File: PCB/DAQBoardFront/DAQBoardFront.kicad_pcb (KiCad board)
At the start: 2 copper layers, 69.8 x 64.2 mm, 35 parts, among them IC2 LMR51430YDDCR, J2 53375-0410, T1 AC1210-110-C, U5 TCAN1051VDRQ1

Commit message: Nearly functional DAQ boards with buck converters and SMD CAN modules
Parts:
- D3, D4, R10, R13, R14, R7, R8, R9, U5: moved to B.Cu
- T1: value AC1210-110-C -> ~; moved to B.Cu
- moved R8 30.4 mm to (141.1, 87.8), turned to 90 degrees
- moved R10 28.3 mm to (143.8, 90.3), turned to 90 degrees
- moved R6 25.7 mm to (138.6, 99.0)
- moved D3 23.0 mm to (143.2, 84.2), turned to 90 degrees
- moved C5 21.2 mm to (141.2, 99.0)
- moved D4 20.9 mm to (145.9, 86.7), turned to 90 degrees
- moved L3 19.8 mm to (141.4, 108.8)
- moved R3 19.8 mm to (141.4, 104.6)
- moved C4 16.1 mm to (143.9, 104.6)
- moved L2 15.4 mm to (143.8, 116.0)
- moved R2 15.4 mm to (143.8, 111.8)
- moved R5 15.0 mm to (138.2, 85.6)
- moved D2 13.9 mm to (140.4, 82.0), turned to 90 degrees
- moved C3 13.8 mm to (145.9, 111.8)
- moved U5 11.5 mm to (114.2, 75.7), turned to 180 degrees
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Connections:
- J1 pad 1: /ExtraAnalog -> /FRSus
- J1 pad 2: /SteeringAngle -> /FLSus
- J1 pad 3: /FLSus -> /SteeringAngle
- J1 pad 4: /FRSus -> /ExtraAnalog
- R13 pad 1: Net-(T1-AB) -> Net-(T1-AA)
- R14 pad 2: Net-(T1-SA) -> Net-(T1-SB)
- T1 pad 1: /CAN Hi -> Net-(T1-AA)
- T1 pad 2: Net-(T1-AB) -> Net-(T1-SB)
- T1 pad 3: Net-(T1-SA) -> /CAN Lo
- T1 pad 4: /CAN Lo -> /CAN Hi
- U5 pad 6: Net-(T1-SA) -> Net-(T1-SB)
- U5 pad 7: Net-(T1-AB) -> Net-(T1-AA)
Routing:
- net /+3.3V: track 5.16 -> 81.3 mm, vias 0 -> 1
- net +5V: track 49.4 -> 79.4 mm
- net /ExtraAnalog: track 74.3 -> 53.5 mm
- net /FLSus: track 58.4 -> 40.8 mm
- net /SteeringAngle: track 63.7 -> 47.5 mm
- net /CAN Hi: track 0.00 -> 14.8 mm
- net /Brake P Input (12V): track 63.5 -> 49.4 mm
- net Net-(D3-A): track 0.00 -> 12.6 mm
- net /CAN Lo: track 0.00 -> 10.5 mm
- net Net-(D4-A): track 0.00 -> 10.5 mm
- net Net-(D2-A): track 5.85 -> 16.1 mm
- net /CANRx: track 12.4 -> 21.3 mm
- net /FLHallEffect: track 55.9 -> 48.3 mm, vias 0 -> 1
- net Net-(T1-AA): track 0.00 -> 5.45 mm
- net Net-(T1-SB): track 0.00 -> 5.45 mm
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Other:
- board size 69.8 x 64.2 mm -> 61.8 x 64.2 mm

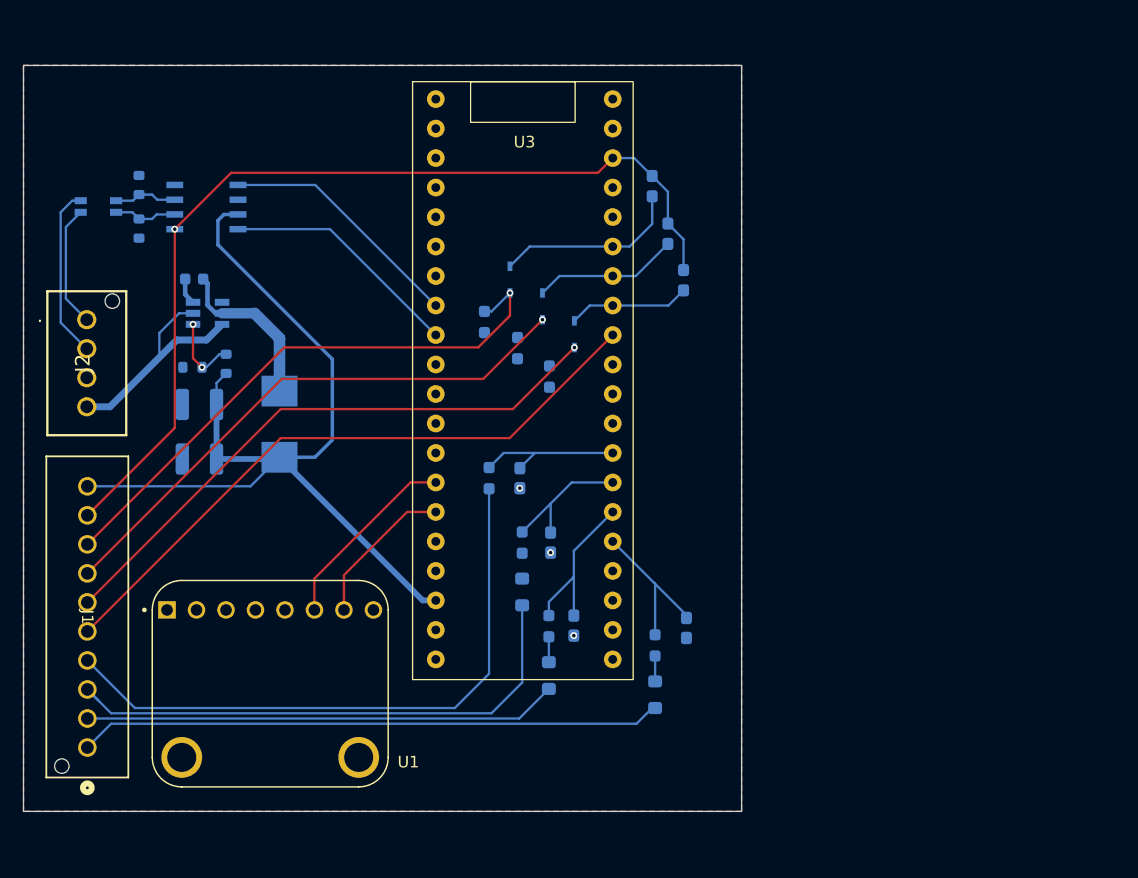
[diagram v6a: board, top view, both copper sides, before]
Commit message: Added schematic design for current sense amplifier
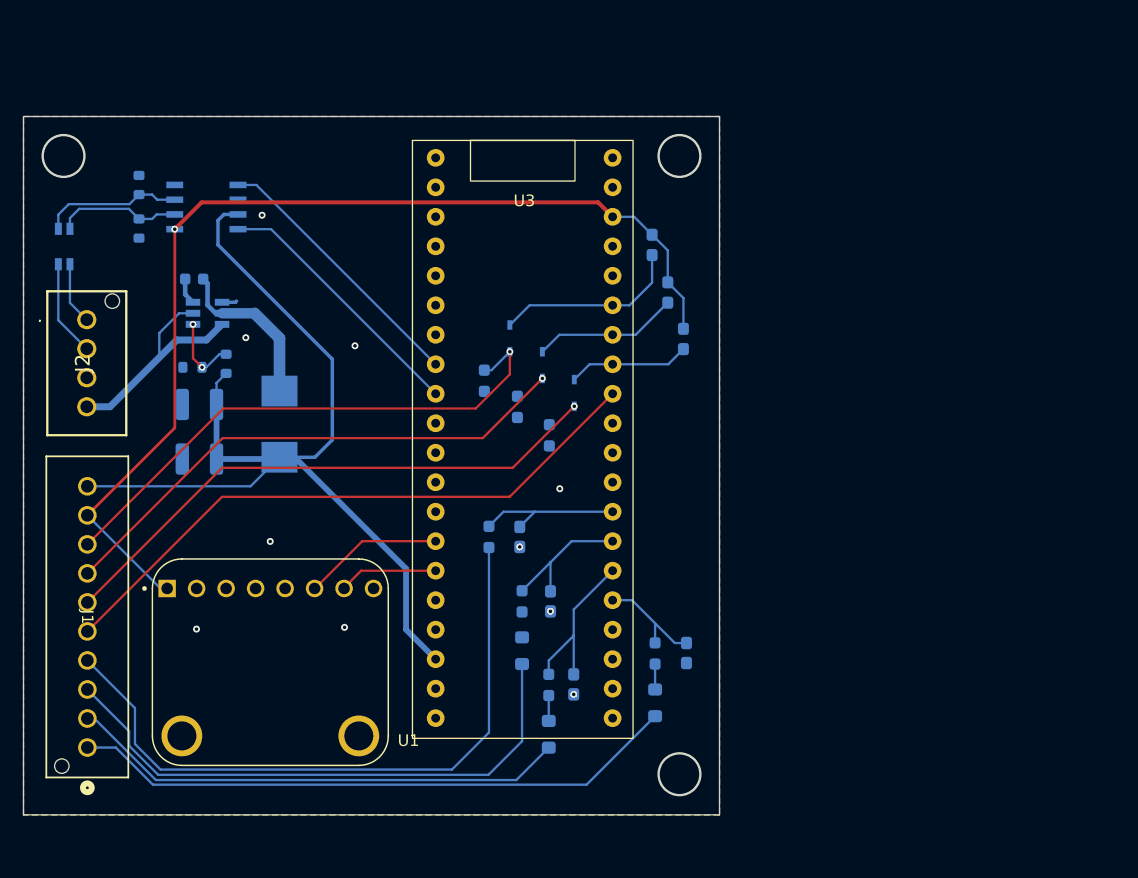
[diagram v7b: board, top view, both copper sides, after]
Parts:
- moved T1 5.53 mm to (101.5, 77.6), turned to -90 degrees
- moved C3 5.06 mm to (145.9, 116.8)
- moved C4 5.06 mm to (143.9, 109.7)
- moved C5 5.06 mm to (141.2, 104.1)
- moved D2 5.06 mm to (140.4, 87.0)
- moved D3 5.06 mm to (143.2, 89.3)
- moved L2 5.06 mm to (143.7, 121.1)
- moved L3 5.06 mm to (141.4, 113.9)
- moved R10 5.06 mm to (143.8, 95.4)
- moved R2 5.06 mm to (143.7, 116.9)
- moved R3 5.06 mm to (141.4, 109.7)
- moved R5 5.06 mm to (138.2, 90.7)
- moved R6 5.06 mm to (138.6, 104.1)
- moved R7 5.06 mm to (154.0, 83.1)
- moved R8 5.06 mm to (141.0, 92.9)
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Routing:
- net /+3.3V: track 81.3 -> 89.7 mm
- net Net-(T1-AA): track 5.45 -> 12.1 mm
- net /CAN Hi: track 14.8 -> 8.29 mm
- net Net-(T1-SB): track 5.45 -> 10.8 mm
- net +5V: track 79.4 -> 84.6 mm
- net /CAN Lo: track 10.5 -> 5.38 mm
- net /Acc SCL: track 16.6 -> 12.1 mm
- net /Acc SDA: track 13.2 -> 8.78 mm
- net /ExtraAnalog: track 53.5 -> 57.6 mm
- net Net-(U3-A0): track 13.7 -> 9.68 mm
- net /FRSus: track 50.3 -> 52.7 mm
- net /FLSus: track 40.8 -> 43.1 mm
- net /Brake P Input (12V): track 49.4 -> 47.3 mm
- net /FRHallEffect: track 51.0 -> 48.9 mm
- net /FLHallEffect: track 48.3 -> 46.1 mm
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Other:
- board size 61.8 x 64.2 mm -> 59.9 x 60.2 mm

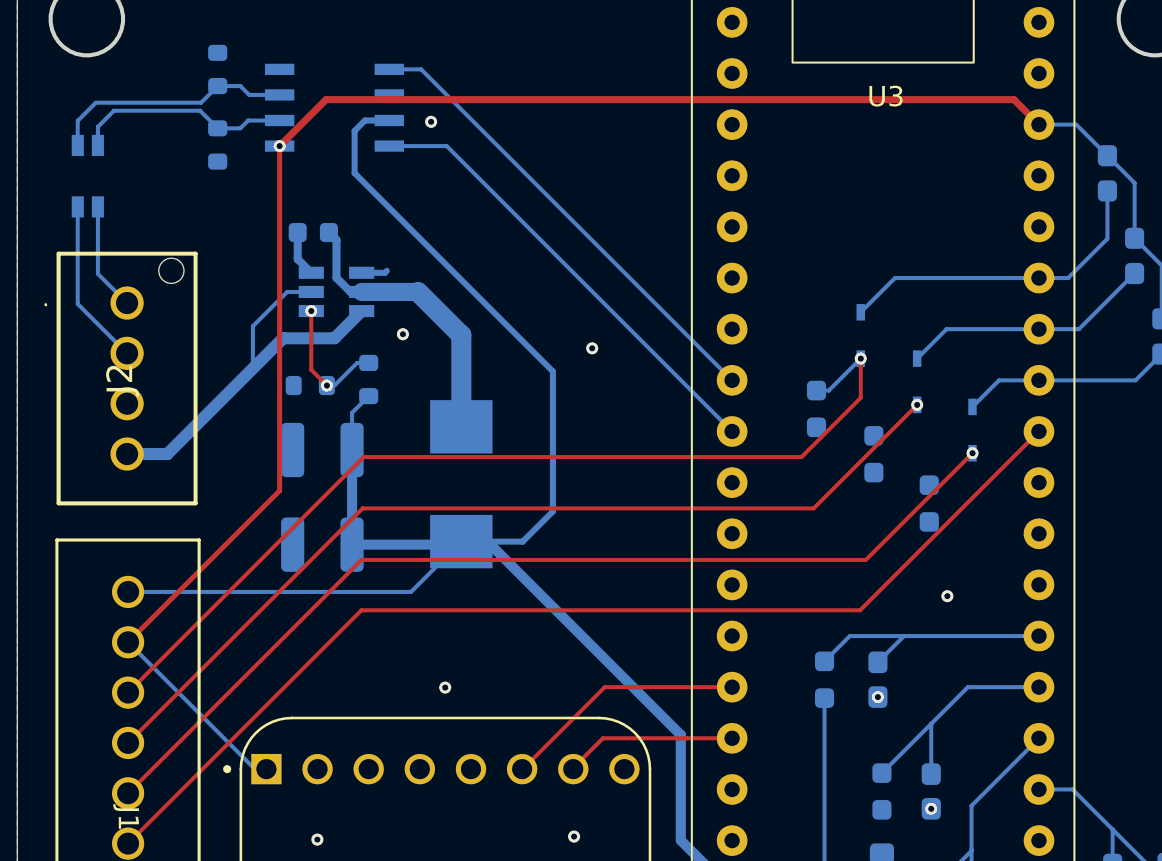
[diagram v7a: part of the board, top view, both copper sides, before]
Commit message: Completed V2.0 of DAQ board, including buck converter, input current measurement, and onboard CAN Transceiver
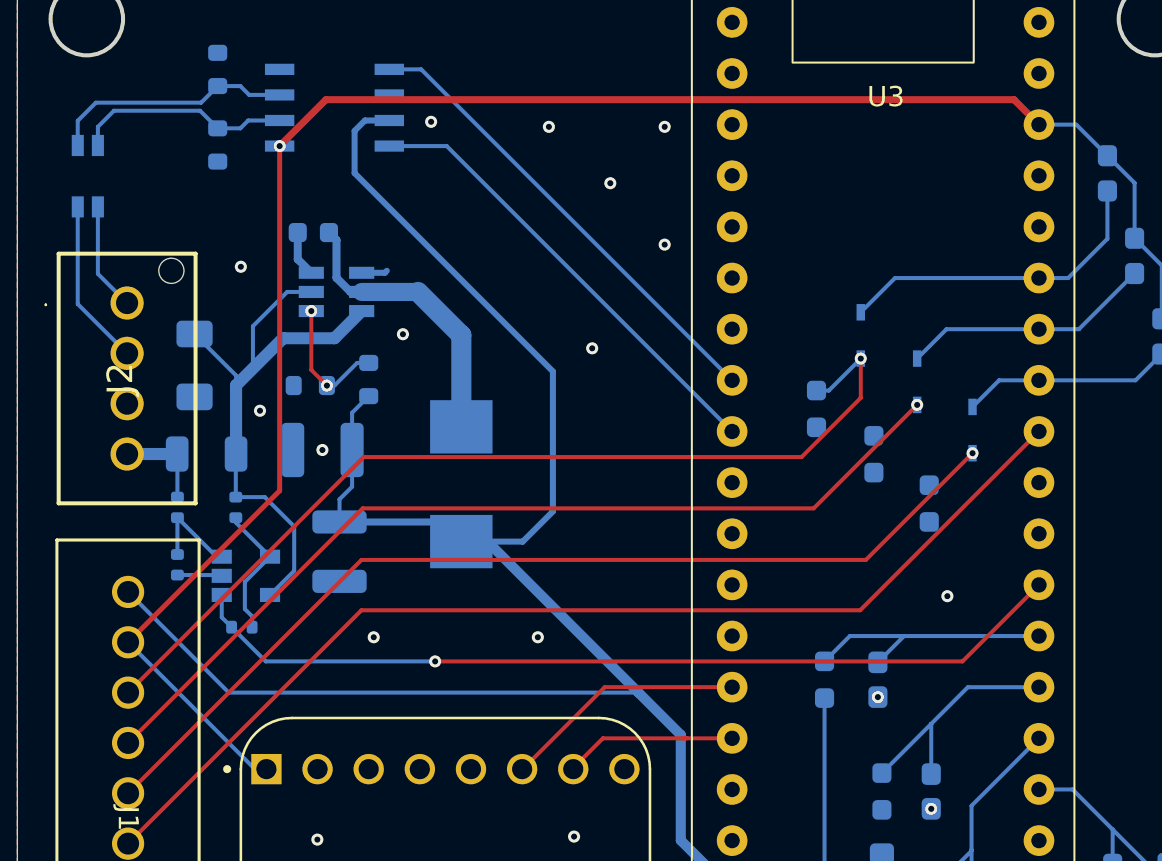
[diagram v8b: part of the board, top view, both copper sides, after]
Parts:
- added C8: C3216X5R1E476M160AC, Capacitor_SMD:C_1206_3216Metric_Pad1.33x1.80mm_HandSolder, B.Cu at (107.3, 88.5)
- added R15: CSR1206FT50L0, Resistor_SMD:R_1206_3216Metric, B.Cu at (107.9, 92.9)
- added R16: 100k, Resistor_SMD:R_0402_1005Metric, B.Cu at (106.5, 95.5)
- added R17: 100k, Resistor_SMD:R_0402_1005Metric, B.Cu at (109.3, 95.5)
- added R18: 22.1k, Resistor_SMD:R_0402_1005Metric, B.Cu at (109.7, 101.5)
- added R19: 56.2k, Resistor_SMD:R_0402_1005Metric, B.Cu at (106.5, 98.4)
- added T2: ~, CFR-Footprint-Library:NCS2005SN1T1G, B.Cu at (108.7, 98.0)
- moved C7 0.92 mm to (114.5, 97.8), turned to -90 degrees
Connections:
- J2 pad 4: /+12V -> /CurrentSense
- U3 pad 29: unconnected-(U3-A4-Pad29) -> /Current_0-3V3
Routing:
- net /Current_0-3V3: track 0.00 -> 44.2 mm, vias 0 -> 1
- net +5V: track 84.6 -> 94.7 mm
- net /+12V: track 20.3 -> 29.8 mm
- net Net-(T2--): track 0.00 -> 6.81 mm
- net Net-(T2-+): track 0.00 -> 4.83 mm
- net /CurrentSense: track 0.00 -> 4.63 mm
- net /GND: track 1.29 -> 3.81 mm, vias 10 -> 18
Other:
- board text removed: "Need to figure out pinout of common-mode choke"
